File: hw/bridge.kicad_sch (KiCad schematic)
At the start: 19 parts, among them J3 MOTOR_A, J4 MOTOR_B, J5 MOTOR_C, Q1 BSC026N08NS5, Q2 BSC026N08NS5, Q3 BSC026N08NS5, Q4 BSC026N08NS5, Q5 BSC026N08NS5, Q6 BSC026N08NS5

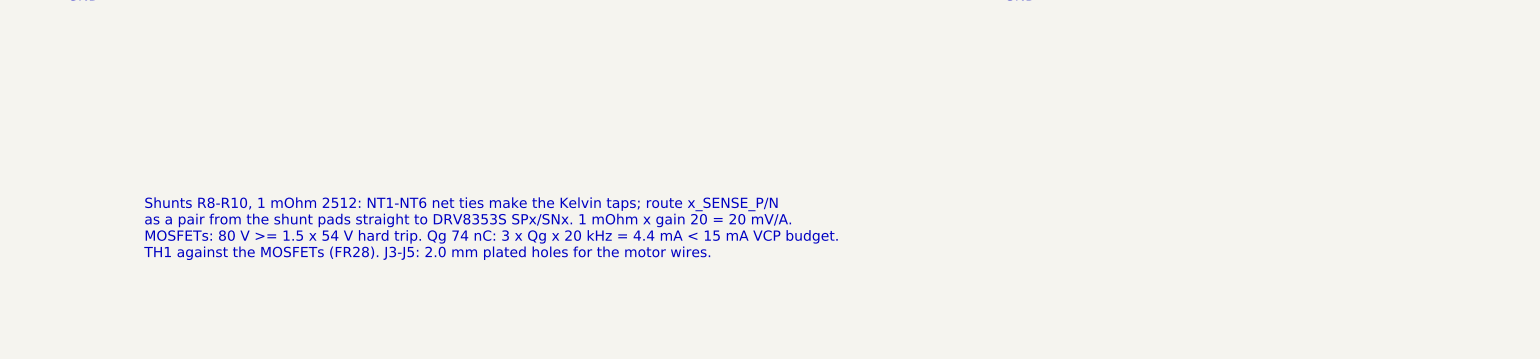
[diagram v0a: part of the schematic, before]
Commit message: Remove requirement IDs from schematic notes
Notes now state the reason in plain words so the schematic reads
without the requirements document.

Co-Authored-By: Claude Opus 5.5 <noreply@anthropic.com>
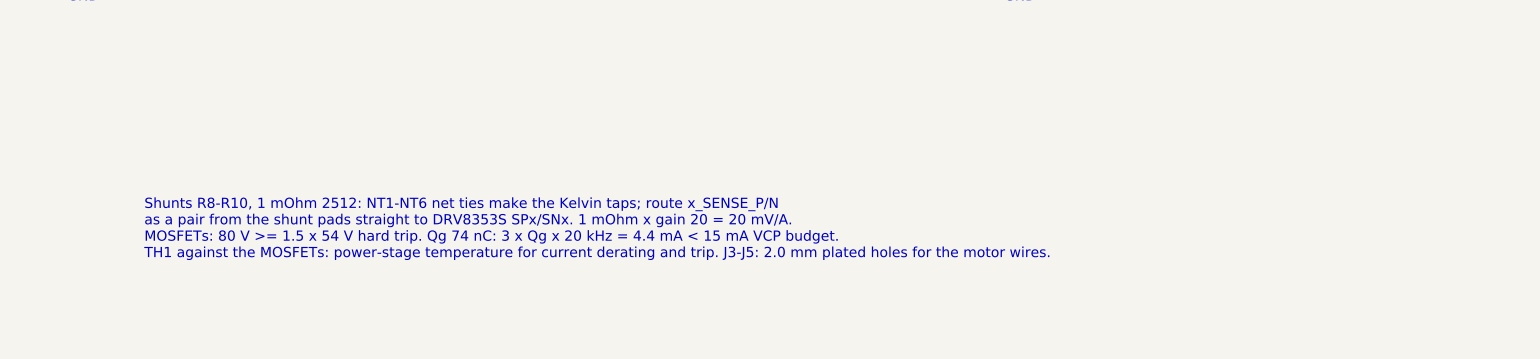
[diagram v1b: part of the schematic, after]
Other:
- note added: "Shunts R8-R10, 1 mOhm 2512: NT1-NT6 net ties make the Kelvin taps; route x_SENSE_P/N as a pair from the shunt pads straight to DRV8353S SPx/SNx. 1 mOhm x gain 20 = 20 mV/A. MOSFETs: 80 V >= 1.5 x 54 V hard trip. Qg 74 nC: 3 x Qg x 20 kHz = 4.4 mA < 15 mA VCP budget. TH1 against the MOSFETs: power-stage temperature for current derating and trip. J3-J5: 2.0 mm plated holes for the motor wires."
- note removed: "Shunts R8-R10, 1 mOhm 2512: NT1-NT6 net ties make the Kelvin taps; route x_SENSE_P/N as a pair from the shunt pads straight to DRV8353S SPx/SNx. 1 mOhm x gain 20 = 20 mV/A. MOSFETs: 80 V >= 1.5 x 54 V hard trip. Qg 74 nC: 3 x Qg x 20 kHz = 4.4 mA < 15 mA VCP budget. TH1 against the MOSFETs (FR28). J3-J5: 2.0 mm plated holes for the motor wires."
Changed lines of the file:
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@@
 		)
 	)
-	(text "Shunts R8-R10, 1 mOhm 2512: NT1-NT6 net ties make the Kelvin taps; route x_SENSE_P/N\nas a pair from the shunt pads straight to DRV8353S SPx/SNx. 1 mOhm x gain 20 = 20 mV/A.\nMOSFETs: 80 V >= 1.5 x 54 V hard trip. Qg 74 nC: 3 x Qg x 20 kHz = 4.4 mA < 15 mA VCP budget.\nTH1 against the MOSFETs (FR28). J3-J5: 2.0 mm plated holes for the motor wires."
+	(text "Shunts R8-R10, 1 mOhm 2512: NT1-NT6 net ties make the Kelvin taps; route x_SENSE_P/N\nas a pair from the shunt pads straight to DRV8353S SPx/SNx. 1 mOhm x gain 20 = 20 mV/A.\nMOSFETs: 80 V >= 1.5 x 54 V hard trip. Qg 74 nC: 3 x Qg x 20 kHz = 4.4 mA < 15 mA VCP budget.\nTH1 against the MOSFETs: power-stage temperature for current derating and trip. J3-J5: 2.0 mm plated holes for the motor wires."
 		(exclude_from_sim no)
 		(at 101.6 210.82 0.0000)

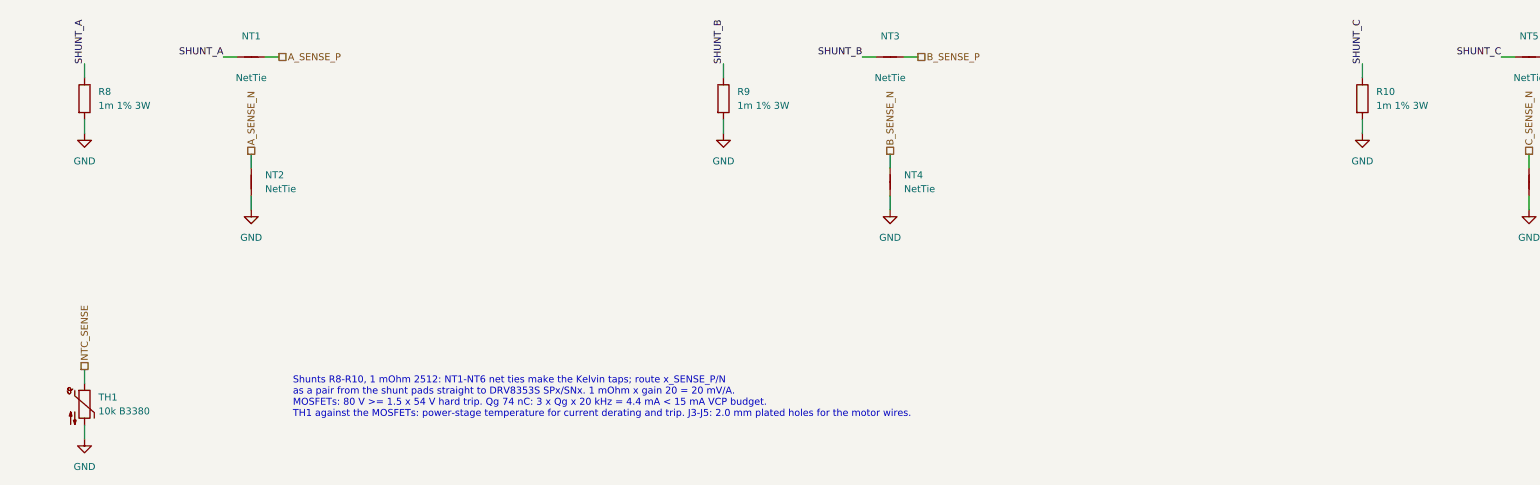
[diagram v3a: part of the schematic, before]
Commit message: Route the 6-layer board and finalize parts for ordering
The 45 x 45 mm board is fully routed on six layers (F / GND / SIG /
SIG / PWR / B, 2 oz outer, 1 oz inner): DRC 0 errors, 0 unconnected,
schematic parity 0. Four layers could not route the DRV-to-MCU links
without moving the power or input stage.

- Encoder shares the DRV8353's SPI3 bus, as on the PoC; PA5-PA7 are
  unused. R25 pulls DRV nSCS up, since the DRV's logic inputs have an
  internal pull-down. The SDO / MISO pin-type warning is an ERC
  exclusion with a note.
- MCU is now the STM32G473CEU6: the G474 without the unused HRTIM,
  checked pin for pin against both datasheets, in stock and cheaper.
- Male XT30PW-M power connectors, HCS1206 shunts, SWD pads at the
  board edge.
- Design doc and review notes updated for the new stack-up, shared
  bus and MCU.

Co-Authored-By: Claude Opus 5.5 <noreply@anthropic.com>
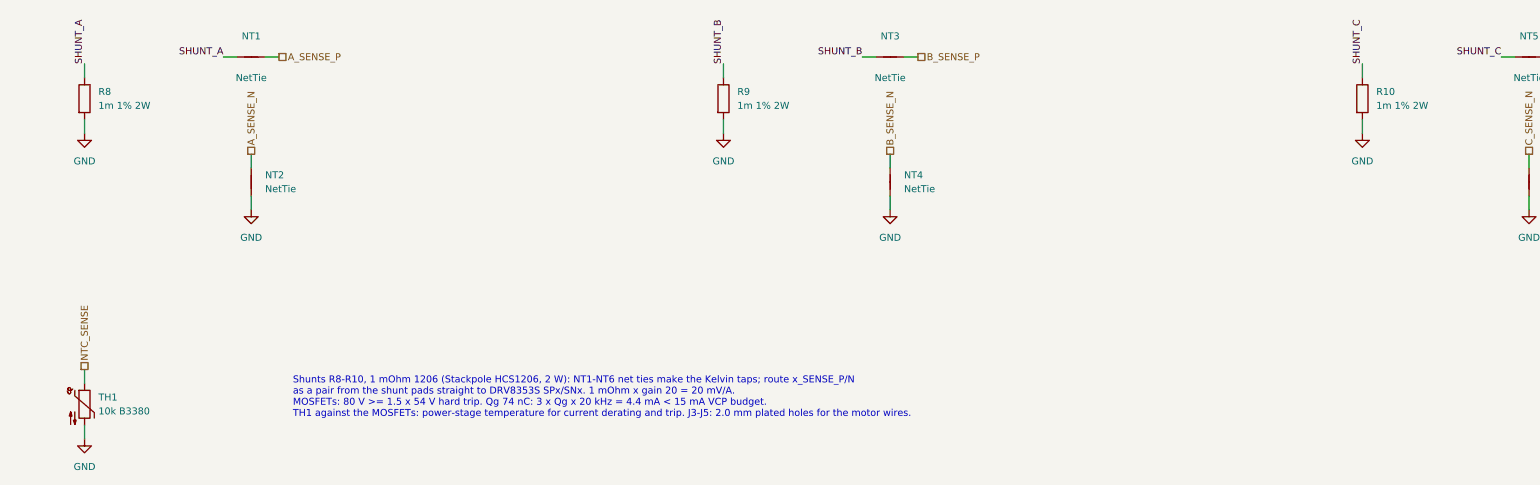
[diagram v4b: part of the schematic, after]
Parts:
- R10, R8, R9: value 1m 1% 3W -> 1m 1% 2W; footprint Resistor_SMD:R_2512_6332Metric -> foc_controller:R_1206_Shunt_HCS1206; LCSC C2903470 -> C4087826; MPN HoJLR2512-3W-1mR-1% -> HCS1206FT1L00
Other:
- note added: "Shunts R8-R10, 1 mOhm 1206 (Stackpole HCS1206, 2 W): NT1-NT6 net ties make the Kelvin taps; route x_SENSE_P/N as a pair from the shunt pads straight to DRV8353S SPx/SNx. 1 mOhm x gain 20 = 20 mV/A. MOSFETs: 80 V >= 1.5 x 54 V hard trip. Qg 74 nC: 3 x Qg x 20 kHz = 4.4 mA < 15 mA VCP budget. TH1 against the MOSFETs: power-stage temperature for current derating and trip. J3-J5: 2.0 mm plated holes 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"
- note removed: "Shunts R8-R10, 1 mOhm 2512: NT1-NT6 net ties make the Kelvin taps; route x_SENSE_P/N as a pair from the shunt pads straight to DRV8353S SPx/SNx. 1 mOhm x gain 20 = 20 mV/A. MOSFETs: 80 V >= 1.5 x 54 V hard trip. Qg 74 nC: 3 x Qg x 20 kHz = 4.4 mA < 15 mA VCP budget. TH1 against the MOSFETs: power-stage temperature for current derating and trip. J3-J5: 2.0 mm plated holes for the motor wires."
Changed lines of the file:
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@@
 		(comment 2 "specs/pmsm-controller/design-electronics.md")
 	)
-	(text "Shunts R8-R10, 1 mOhm 2512: NT1-NT6 net ties make the Kelvin taps; route x_SENSE_P/N\nas a pair from the shunt pads straight to DRV8353S SPx/SNx. 1 mOhm x gain 20 = 20 mV/A.\nMOSFETs: 80 V >= 1.5 x 54 V hard trip. Qg 74 nC: 3 x Qg x 20 kHz = 4.4 mA < 15 mA VCP budget.\nTH1 against the MOSFETs: power-stage temperature for current derating and trip. J3-J5: 2.0 mm plated holes for the motor wires."
+	(text "Shunts R8-R10, 1 mOhm 1206 (Stackpole HCS1206, 2 W): NT1-NT6 net ties make the Kelvin taps; route x_SENSE_P/N\nas a pair from the shunt pads straight to DRV8353S SPx/SNx. 1 mOhm x gain 20 = 20 mV/A.\nMOSFETs: 80 V >= 1.5 x 54 V hard trip. Qg 74 nC: 3 x Qg x 20 kHz = 4.4 mA < 15 mA VCP budget.\nTH1 against the MOSFETs: power-stage temperature for current derating and trip. J3-J5: 2.0 mm plated holes for the motor wires."
 		(exclude_from_sim no)
 		(at 101.6 210.82 0)
@@
 			)
 		)
-		(property "Value" "1m 1% 3W"
+		(property "Value" "1m 1% 2W"
 			(at 66.04 161.29 0)
 			(show_name no)
@@
 			)
 		)
-		(property "Footprint" "Resistor_SMD:R_2512_6332Metric"
+		(property "Footprint" "foc_controller:R_1206_Shunt_HCS1206"
 			(at 61.722 160.02 90)
 			(hide yes)
@@
 			)
 		)
-		(property "LCSC" "C2903470"
+		(property "LCSC" "C4087826"
 			(at 66.04 165.0999 0)
 			(hide yes)
@@
 			)
 		)
-		(property "MPN" "HoJLR2512-3W-1mR-1%"
+		(property "MPN" "HCS1206FT1L00"
 			(at 66.04 165.0999 0)
 			(hide yes)
@@
 			)
 		)
-		(property "Value" "1m 1% 3W"
+		(property "Value" "1m 1% 2W"
 			(at 299.72 161.29 0)
 			(show_name no)
@@
 			)
 		)
-		(property "Footprint" "Resistor_SMD:R_2512_6332Metric"
+		(property "Footprint" "foc_controller:R_1206_Shunt_HCS1206"
 			(at 295.402 160.02 90)
 			(hide yes)
@@
 			)
 		)
-		(property "LCSC" "C2903470"
+		(property "LCSC" "C4087826"
 			(at 299.72 165.0999 0)
 			(hide yes)
@@
 			)
 		)
-		(property "MPN" "HoJLR2512-3W-1mR-1%"
+		(property "MPN" "HCS1206FT1L00"
 			(at 299.72 165.0999 0)
 			(hide yes)
@@
 			)
 		)
-		(property "Value" "1m 1% 3W"
+		(property "Value" "1m 1% 2W"
 			(at 182.88 161.29 0)
 			(show_name no)
@@
 			)
 		)
-		(property "Footprint" "Resistor_SMD:R_2512_6332Metric"
+		(property "Footprint" "foc_controller:R_1206_Shunt_HCS1206"
 			(at 178.562 160.02 90)
 			(hide yes)
@@
 			)
 		)
-		(property "LCSC" "C2903470"
+		(property "LCSC" "C4087826"
 			(at 182.88 165.0999 0)
 			(hide yes)
@@
 			)
 		)
-		(property "MPN" "HoJLR2512-3W-1mR-1%"
+		(property "MPN" "HCS1206FT1L00"
 			(at 182.88 165.0999 0)
 			(hide yes)
